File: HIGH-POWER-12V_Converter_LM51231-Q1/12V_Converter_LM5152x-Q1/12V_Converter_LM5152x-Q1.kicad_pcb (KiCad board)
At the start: 2 copper layers, 42.1 x 41.3 mm, 34 parts, among them M1 60V, M2 60V, U1 LM51521QRGRRQ1

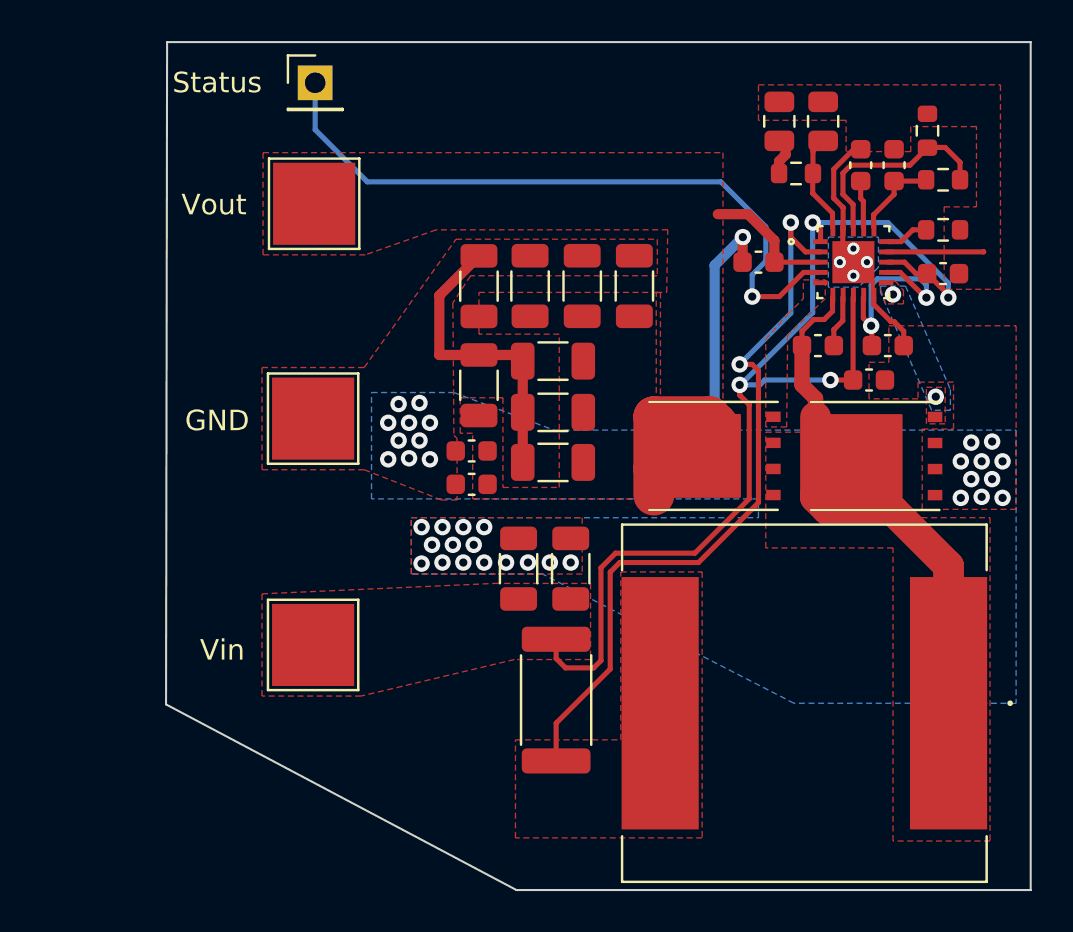
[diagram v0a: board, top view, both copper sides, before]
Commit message: updated from reviews
- changed capacitor
- changed output capacitors
- moved a bunch of stuff around and filled in a lot of copper area
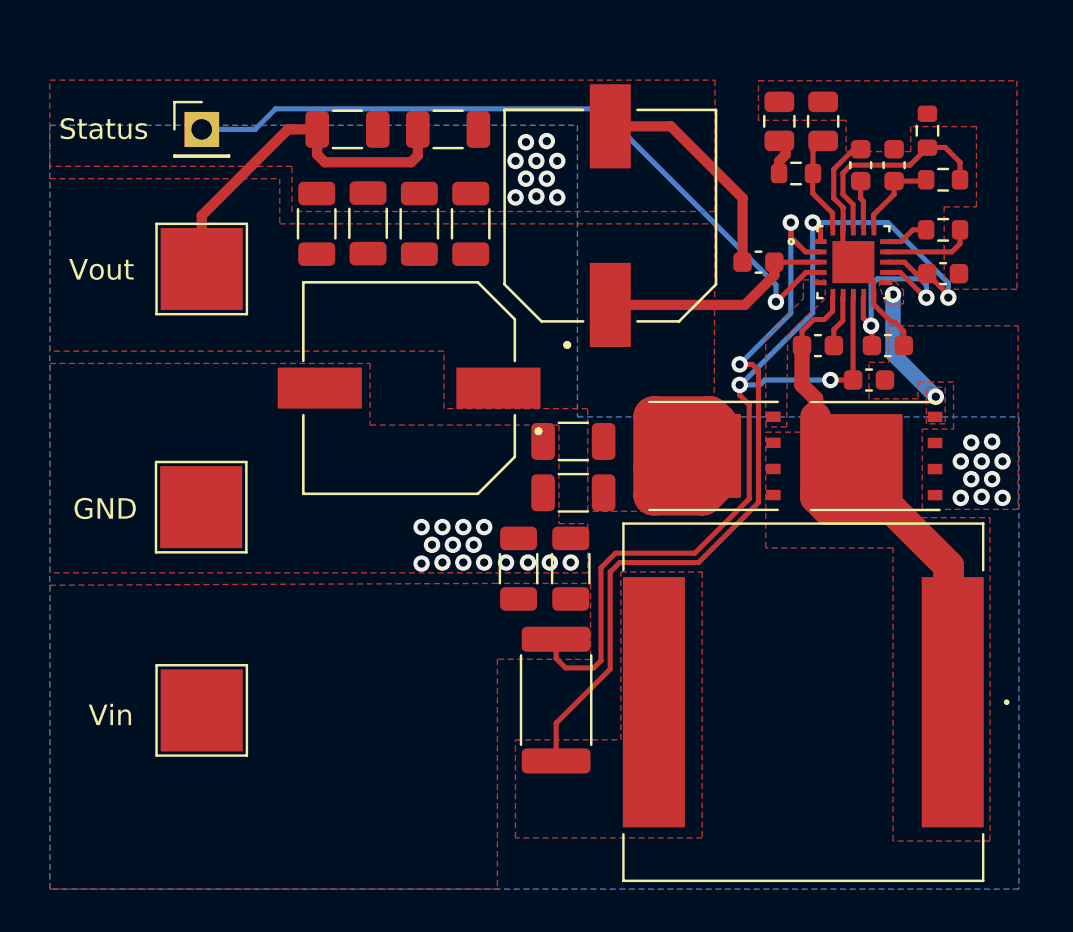
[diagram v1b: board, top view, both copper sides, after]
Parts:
- Cout1, Cout2: footprint Capacitor_SMD:C_0603_1608Metric -> 270u_cap:CAP_EEHZS1H271UP
- L1: value 2.2u -> 2.2; footprint inductor:HCMA1707-330-R -> inductor2.2:IHLP6767GZER2R2M51
- moved Cout1 13.3 mm to (89.1, 97.2), turned to 90 degrees
- moved Coutx4 11.2 mm to (77.3, 97.6), turned to -90 degrees
- moved Coutx3 11.1 mm to (74.8, 97.6)
- moved Coutx6 10.9 mm to (79.8, 97.6)
- moved Coutx5 9.96 mm to (76.3, 93.0), turned to 180 degrees
- moved Coutx8 8.61 mm to (81.2, 93.0), turned to 180 degrees
- moved REF** 6.95 mm to (69.2, 111.4)
- moved REF** 6.33 mm to (69.2, 99.8)
- moved REF** 6.29 mm to (69.2, 121.3)
- moved Coutx7 6.22 mm to (82.3, 97.6)
- moved Status 5.98 mm to (69.2, 93.0)
- moved Cout2 5.59 mm to (79.3, 105.6), turned to 180 degrees
- moved Coutx1 1.78 mm to (87.3, 110.7)
- moved Coutx2 1.73 mm to (87.3, 108.2)
- moved L1 0.07 mm to (98.5, 120.9)
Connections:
- Cout1 pad 1: GND -> Vout
- Cout1 pad 2: Vout -> GND
- Cout2 pad 1: GND -> Vout
- Cout2 pad 2: Vout -> GND
- REF** pad 1: (no net) -> Vout
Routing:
- net Vout: track 18.1 -> 46.7 mm
- net GND: track 43.1 -> 27.3 mm, vias 40 -> 35
- net Net-(M1-Pad4): track 0.00 -> 5.84 mm
- net status: track 33.6 -> 35.4 mm
- net Net-(Cbst1-Pad2): track 25.7 -> 25.0 mm
- removed copper zone on B.Cu, net Net-(M1-Pad4)
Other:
- board outline removed
